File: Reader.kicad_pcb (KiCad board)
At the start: 2 copper layers, 40.4 x 60 mm, 39 parts, among them J1 Conn_01x04, J2 Amphenol Dubox ‎76383-402LF‎, J3 Conn_01x04, J4 Conn_01x08, J5 Conn_01x10, J6 Conn_01x03, J7 Conn_01x02, Q1 2N7002, Q2 2N7002, Q3 2N7002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

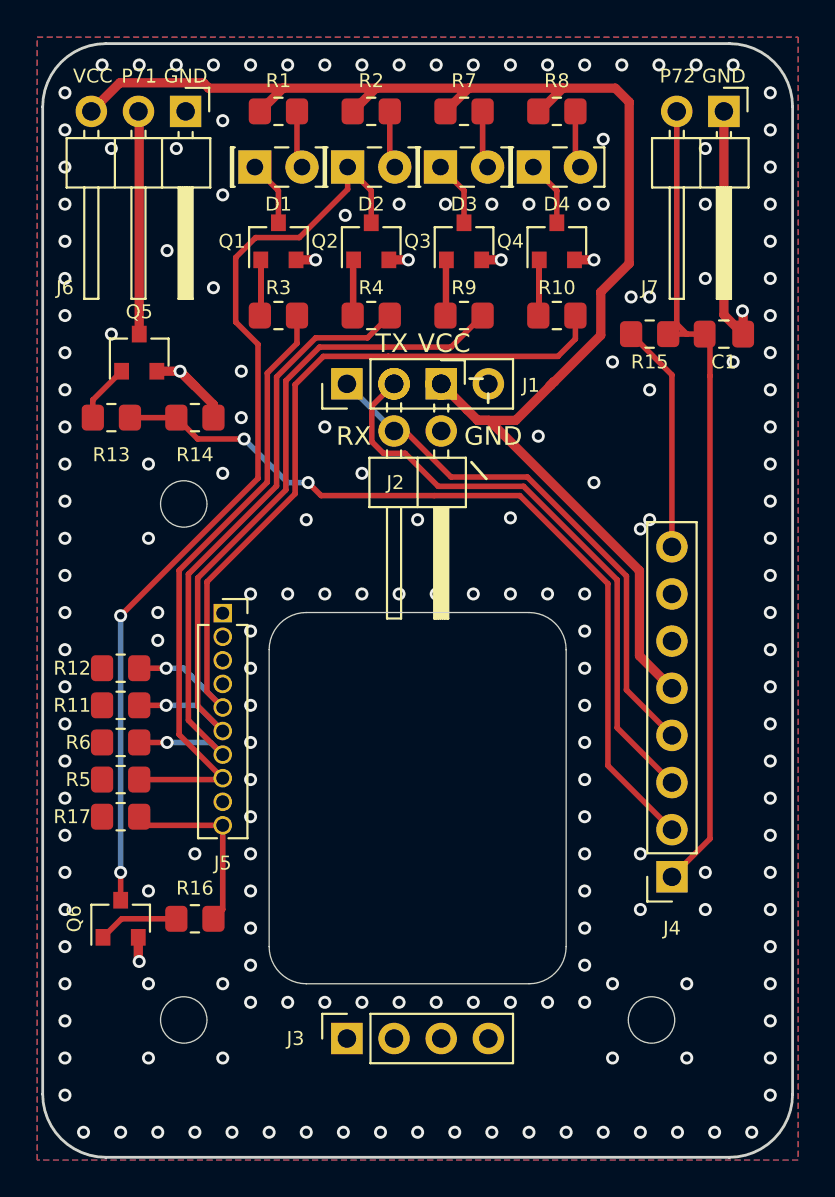
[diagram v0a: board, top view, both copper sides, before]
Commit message: Update schematic to KiCad 7
This also sets the edge clearance to 0,5mm. This is a new setting, that
was previously set using edge cuts line widths and/or zone clearance
settings. This commit also refills the zones, which are slightly bigger
than before.

This also removes the old .sch and .pro file, which are replaced by
.kicad_sch and .kicad_pro, and removes the lib cache, which is no longer
used in the new schematic format.
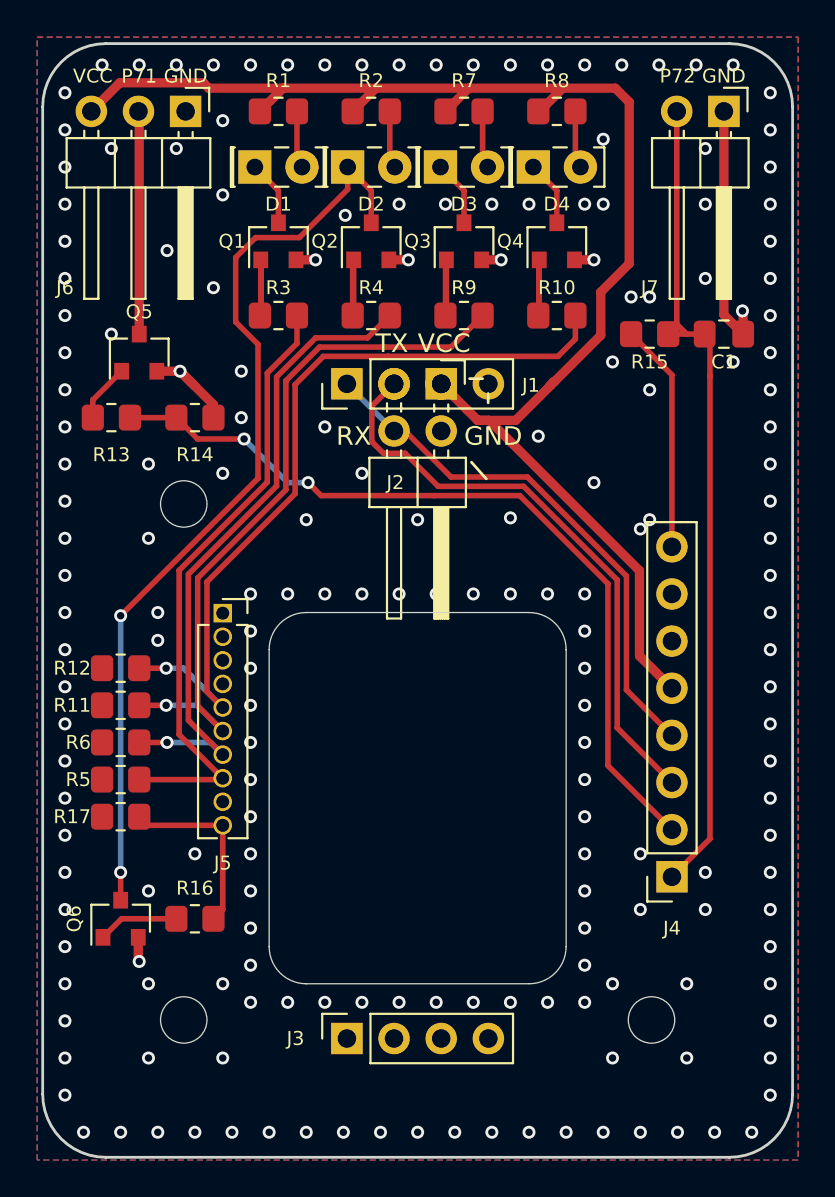
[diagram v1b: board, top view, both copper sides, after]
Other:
- outline, holes or cut-outs redrawn
- net class Bigger removed
- net class Default removed
- net class Minimal removed
- net class Power removed

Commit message: Add board name and version to front silkscreen
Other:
- board text added: "Doorlockd reader v0.1"
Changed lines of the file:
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@@
     (effects (font (size 0.75 0.75) (thickness 0.1)))
+  )
+  (gr_text "Doorlockd\nreader v0.1" (at 113.5 82.5) (layer "F.SilkS")
+    (effects (font (size 1 1) (thickness 0.15)))
   )
   (gr_text "GND" (at 102.5 82.5) (layer "F.SilkS")

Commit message: Update PCB from schematic
This makes no actual changes, just lets KiCad pull in changes (probably
mostly udpated footprints and renumbered symbols, and maybe some KiCad
upgrade changes too).
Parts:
- removed REF**: OSHW-Logo2_9.8x8mm_SilkScreen, Symbol:OSHW-Logo2_9.8x8mm_SilkScreen
- R1, R2, R8: value R -> 100R
- R11, R12, R14, R17, R5, R6: value 10k -> 1k
- R7: value R -> 200R

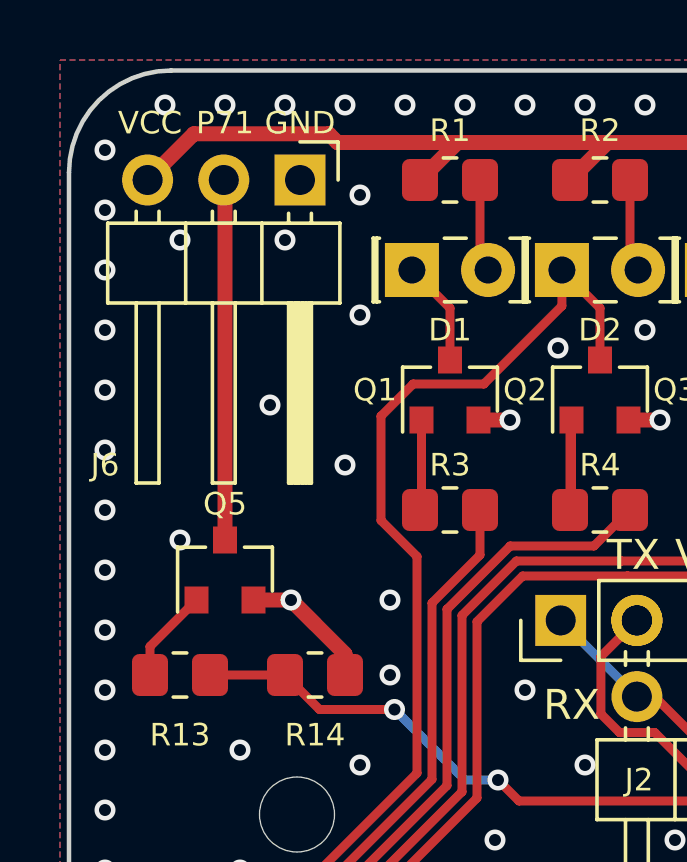
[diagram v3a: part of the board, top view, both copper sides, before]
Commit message: Add 100n capacitor on output pin
This takes care of suppressing the startup pulse given by the PN532.
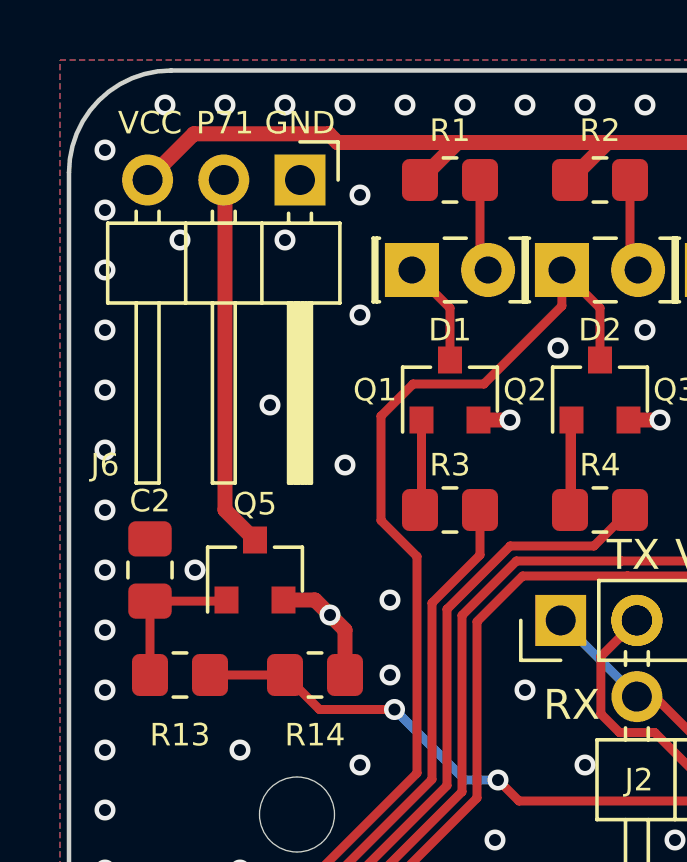
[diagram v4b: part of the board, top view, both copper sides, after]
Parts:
- added C2: 100n, Capacitor_SMD:C_0805_2012Metric_Pad1.18x1.45mm_HandSolder, F.Cu at (82.5, 78.0)
- moved Q5 1.00 mm to (86.0, 78.0)
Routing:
- net Net-(Q5-G): track 3.14 -> 5.08 mm
- net GND: track 24.9 -> 23.2 mm
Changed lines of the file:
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@@
   )
   (footprint "Package_TO_SOT_SMD:SOT-23" (layer "F.Cu")
-    (at 85 78 90)
+    (at 86 78 90)
     (descr "SOT-23, Standard")
     (tags "SOT-23")
@@
       (net 1 "GND") (pintype "passive"))
     (model "${KISYS3DMOD}/Resistor_SMD.3dshapes/R_0805_2012Metric.wrl"
+      (offset (xyz 0 0 0))
+      (scale (xyz 1 1 1))
+      (rotate (xyz 0 0 0))
+    )
+  )
+  (footprint "Capacitor_SMD:C_0805_2012Metric_Pad1.18x1.45mm_HandSolder" (layer "F.Cu")
+    (at 82.5 78 90)
+    (descr "Capacitor SMD 0805 (2012 Metric), square (rectangular) end terminal, IPC_7351 nominal with elongated pad for handsoldering. (Body size source: IPC-SM-782 page 76, https://www.pcb-3d.com/wordpress/wp-content/uploads/ipc-sm-782a_amendment_1_and_2.pdf, https://docs.google.com/spreadsheets/d/1BsfQQcO9C6DZCsRaXUlFlo91Tg2WpOkGARC1WS5S8t0/edit?usp=sharing), generated with kicad-footprint-generator")
+    (tags "capacitor handsolder")
+    (property "Sheetfile" "Reader.kicad_sch")
+    (property "Sheetname" "")
+    (property "ki_description" "Unpolarized capacitor")
+    (property "ki_keywords" "cap capacitor")
+    (attr smd)
+    (fp_text reference "C2" (at 2.3 0 180) (layer "F.SilkS")
+        (effects (font (size 0.75 0.75) (thickness 0.1)))
+    )
+    (fp_text value "100n" (at 1.7 -0.6 180) (layer "F.Fab")
+        (effects (font (size 1 1) (thickness 0.15)))
+    )
+    (fp_text user "${REFERENCE}" (at 0 0 90) (layer "F.Fab")
+        (effects (font (size 0.5 0.5) (thickness 0.08)))
+    )
+    (fp_line (start -0.261252 -0.735) (end 0.261252 -0.735)
+      (stroke (width 0.12) (type solid)) (layer "F.SilkS"))
+    (fp_line (start -0.261252 0.735) (end 0.261252 0.735)
+      (stroke (width 0.12) (type solid)) (layer "F.SilkS"))
+    (fp_line (start -1.88 -0.98) (end 1.88 -0.98)
+      (stroke (width 0.05) (type solid)) (layer "F.CrtYd"))
+    (fp_line (start -1.88 0.98) (end -1.88 -0.98)
+      (stroke (width 0.05) (type solid)) (layer "F.CrtYd"))
+    (fp_line (start 1.88 -0.98) (end 1.88 0.98)
+      (stroke (width 0.05) (type solid)) (layer "F.CrtYd"))
+    (fp_line (start 1.88 0.98) (end -1.88 0.98)
+      (stroke (width 0.05) (type solid)) (layer "F.CrtYd"))
+    (fp_line (start -1 -0.625) (end 1 -0.625)
+      (stroke (width 0.1) (type solid)) (layer "F.Fab"))
+    (fp_line (start -1 0.625) (end -1 -0.625)
+      (stroke (width 0.1) (type solid)) (layer "F.Fab"))
+    (fp_line (start 1 -0.625) (end 1 0.625)
+      (stroke (width 0.1) (type solid)) (layer "F.Fab"))
+    (fp_line (start 1 0.625) (end -1 0.625)
+      (stroke (width 0.1) (type solid)) (layer "F.Fab"))
+    (pad "1" smd roundrect (at -1.0375 0 90) (size 1.175 1.45) (layers "F.Cu" "F.Paste" "F.Mask") (roundrect_rratio 0.212766)
+      (net 34 "Net-(Q5-G)") (pintype "passive"))
+    (pad "2" smd roundrect (at 1.0375 0 90) (size 1.175 1.45) (layers "F.Cu" "F.Paste" "F.Mask") (roundrect_rratio 0.212766)
+      (net 1 "GND") (pintype "passive"))
+    (model "${KICAD6_3DMODEL_DIR}/Capacitor_SMD.3dshapes/C_0805_2012Metric.wrl"
       (offset (xyz 0 0 0))
       (scale (xyz 1 1 1))
@@
     (style (thickness 0.15) (arrow_length 1.27) (text_position_mode 0) (extension_height 0.58642) (extension_offset 0) keep_text_aligned)
   )
+  (segment (start 89 80) (end 89 81.5) (width 0.5) (layer "F.Cu") (net 1))
+  (segment (start 88 79) (end 88.5 79.5) (width 0.5) (layer "F.Cu") (net 1))
+  (segment (start 88.5 79.5) (end 89 80) (width 0.5) (layer "F.Cu") (net 1))
+  (segment (start 86.95 79) (end 88 79) (width 0.5) (layer "F.Cu") (net 1))
   (segment (start 84.95 109.5) (end 84.95 110.75) (width 0.5) (layer "F.Cu") (net 1))
-  (segment (start 85.95 79) (end 87.2 79) (width 0.5) (layer "F.Cu") (net 1))
-  (segment (start 89 80.8) (end 87.2 79) (width 0.5) (layer "F.Cu") (net 1))
   (segment (start 116.5 75.9625) (end 117.5375 77) (width 0.5) (layer "F.Cu") (net 1))
   (segment (start 84.95 110.75) (end 85 110.8) (width 0.5) (layer "F.Cu") (net 1))
   (segment (start 98.45 73) (end 98.5 73) (width 0.5) (layer "F.Cu") (net 1))
-  (segment (start 89 81.5) (end 89 80.8) (width 0.5) (layer "F.Cu") (net 1))
-  (segment (start 87.2 79.05) (end 87.2 79) (width 0.5) (layer "F.Cu") (net 1))
   (segment (start 93.45 73) (end 94.5 73) (width 0.5) (layer "F.Cu") (net 1))
   (segment (start 117.5375 77) (end 117.5375 75.7875) (width 0.5) (layer "F.Cu") (net 1))
   (segment (start 98.5 73) (end 99.5 73) (width 0.5) (layer "F.Cu") (net 1))
-  (segment (start 88 79.8) (end 87.2 79) (width 0.5) (layer "F.Cu") (net 1))
   (segment (start 108.45 73) (end 109.5 73) (width 0.5) (layer "F.Cu") (net 1))
   (segment (start 116.5 65) (end 116.5 75.9625) (width 0.5) (layer "F.Cu") (net 1))
@@
   (via (at 81 82) (size 0.7) (drill 0.4) (layers "F.Cu" "B.Cu") (net 1))
   (via (at 109 99) (size 0.7) (drill 0.4) (layers "F.Cu" "B.Cu") (net 1))
+  (via (at 88.5 79.5) (size 0.7) (drill 0.4) (layers "F.Cu" "B.Cu") (net 1))
   (via (at 92 120) (size 0.7) (drill 0.4) (layers "F.Cu" "B.Cu") (net 1))
   (via (at 101 62.5) (size 0.7) (drill 0.4) (layers "F.Cu" "B.Cu") (net 1))
@@
   (via (at 81 104) (size 0.7) (drill 0.4) (layers "F.Cu" "B.Cu") (net 1))
   (via (at 85 62.5) (size 0.7) (drill 0.4) (layers "F.Cu" "B.Cu") (net 1))
-  (via (at 87.2 79) (size 0.7) (drill 0.4) (layers "F.Cu" "B.Cu") (net 1))
   (via (at 101 91) (size 0.7) (drill 0.4) (layers "F.Cu" "B.Cu") (net 1))
   (via (at 119 64) (size 0.7) (drill 0.4) (layers "F.Cu" "B.Cu") (net 1))
@@
   (via (at 100 87) (size 0.7) (drill 0.4) (layers "F.Cu" "B.Cu") (net 1))
   (via (at 81 106) (size 0.7) (drill 0.4) (layers "F.Cu" "B.Cu") (net 1))
-  (via (at 83.5 77) (size 0.7) (drill 0.4) (layers "F.Cu" "B.Cu") (net 1))
+  (via (at 84 78) (size 0.7) (drill 0.4) (layers "F.Cu" "B.Cu") (net 1))
   (via (at 115.5 67) (size 0.7) (drill 0.4) (layers "F.Cu" "B.Cu") (net 1))
   (via (at 119 78) (size 0.7) (drill 0.4) (layers "F.Cu" "B.Cu") (net 1))
@@
   (segment (start 107.818622 63.74999) (end 102.75001 63.74999) (width 0.5) (layer "F.Cu") (net 28))
   (segment (start 113.7 96.08) (end 111.950012 94.330012) (width 0.5) (layer "F.Cu") (net 28))
+  (segment (start 86 77) (end 85 76) (width 0.5) (layer "F.Cu") (net 29))
   (segment (start 85 65.04) (end 84.96 65) (width 0.5) (layer "F.Cu") (net 29))
-  (segment (start 85 77) (end 85 65.04) (width 0.5) (layer "F.Cu") (net 29))
+  (segment (start 85 76) (end 85 65.04) (width 0.5) (layer "F.Cu") (net 29))
   (segment (start 91.55 76.45) (end 91.5 76.5) (width 0.3) (layer "F.Cu") (net 30))
   (segment (start 91.55 73) (end 91.55 76.45) (width 0.3) (layer "F.Cu") (net 30))
@@
   (segment (start 106.55 75.95) (end 106.5 76) (width 0.3) (layer "F.Cu") (net 33))
   (segment (start 106.55 76.45) (end 106.5 76.5) (width 0.3) (layer "F.Cu") (net 33))
-  (segment (start 82.5 80.55) (end 84.05 79) (width 0.3) (layer "F.Cu") (net 34))
-  (segment (start 82.5 81.5) (end 82.5 80.55) (width 0.3) (layer "F.Cu") (net 34))
+  (segment (start 85.0125 79.0375) (end 85.05 79) (width 0.3) (layer "F.Cu") (net 34))
+  (segment (start 82.5 79.0375) (end 85.0125 79.0375) (width 0.3) (layer "F.Cu") (net 34))
+  (segment (start 82.5 79.0375) (end 82.5 81.5) (width 0.3) (layer "F.Cu") (net 34))
+  (segment (start 85 79) (end 85.05 79) (width 0.3) (layer "F.Cu") (net 34))
   (segment (start 84.05 108.5) (end 83.05 109.5) (width 0.3) (layer "F.Cu") (net 36))
   (segment (start 87 108.5) (end 84.05 108.5) (width 0.3) (layer "F.Cu") (net 36))

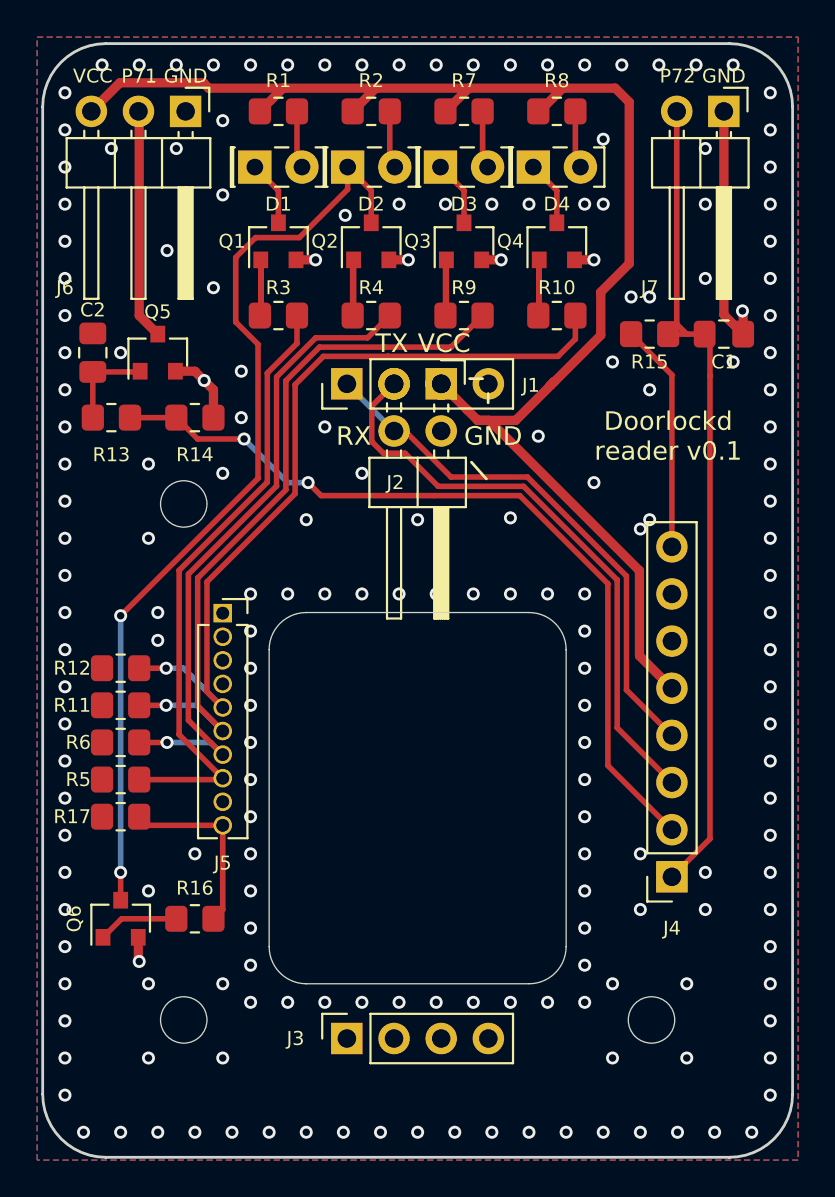
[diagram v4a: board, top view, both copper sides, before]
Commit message: Add series resistors for button input
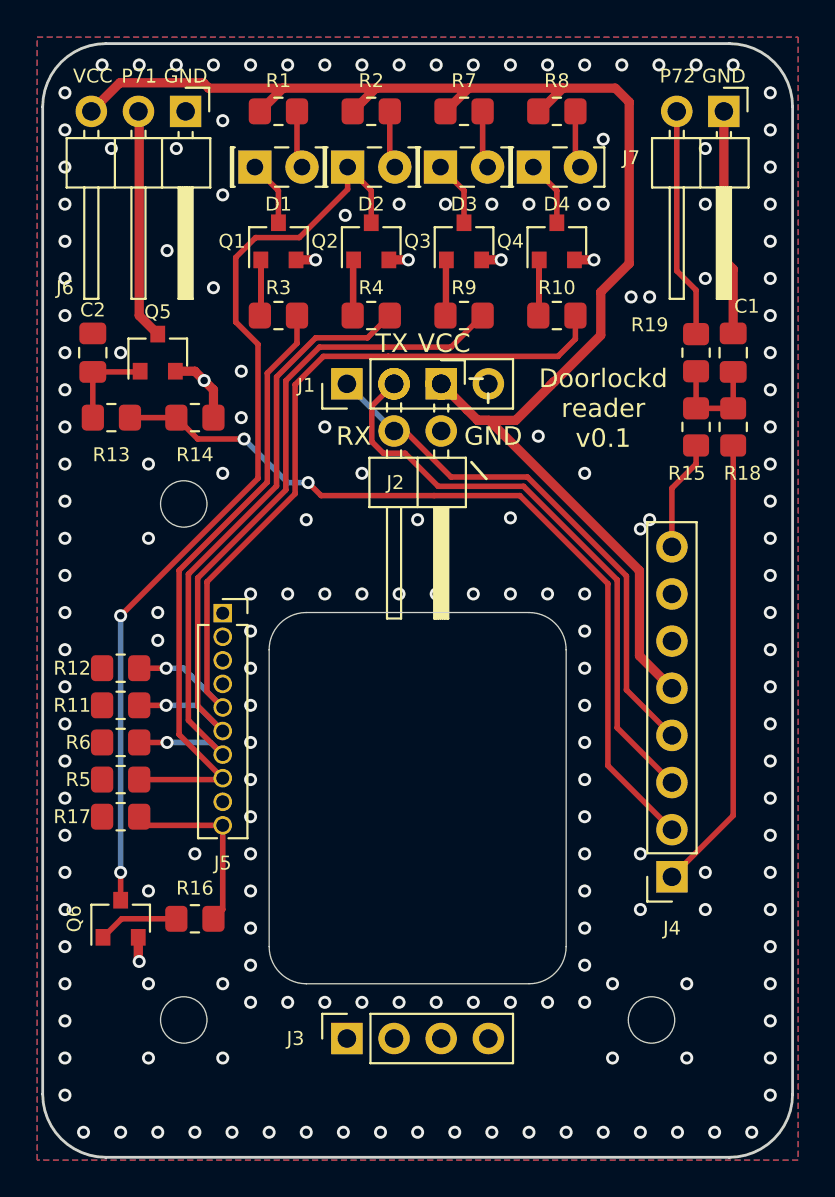
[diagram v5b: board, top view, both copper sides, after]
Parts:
- added R18: 1k, Resistor_SMD:R_0805_2012Metric_Pad1.20x1.40mm_HandSolder, F.Cu at (117.0, 82.0)
- added R19: 100R, Resistor_SMD:R_0805_2012Metric_Pad1.20x1.40mm_HandSolder, F.Cu at (115.0, 78.0)
- moved R15 5.59 mm to (115.0, 82.0), turned to 90 degrees
- moved C1 1.12 mm to (117.0, 78.0), turned to 90 degrees
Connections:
- C1 pad 1: P72 -> Net-(C1-Pad1)
- J7 pad 2: P72 -> Net-(J7-Pin_2)
- R15 pad 2: P72 -> Net-(C1-Pad1)
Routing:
- net P72: track 44.5 -> 24.6 mm
- net Net-(J7-Pin_2): track 0.00 -> 12.4 mm
- net RSTOUT_N: track 12.4 -> 6.00 mm
- net Net-(C1-Pad1): track 0.00 -> 5.96 mm
- net GND: track 23.2 -> 21.7 mm, vias 193 -> 189

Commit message: Enlarge mounting holes
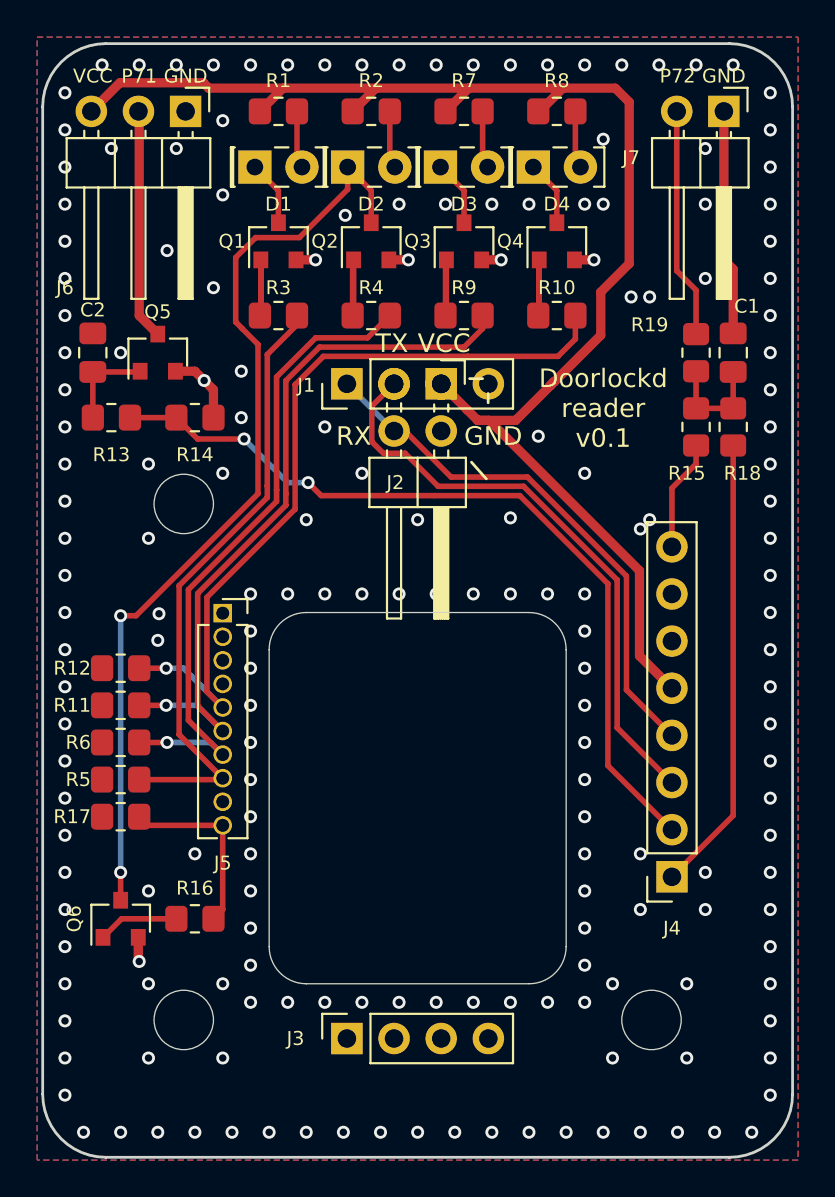
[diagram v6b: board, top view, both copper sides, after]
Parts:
- H1, H2, H3: footprint MountingHole:MountingHole_2.5mm -> MountingHole:MountingHole_3.2mm_M3
